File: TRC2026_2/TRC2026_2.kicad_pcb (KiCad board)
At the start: 2 copper layers, 79 x 180 mm, 31 parts, among them J1 Conn_01x02_Pin, J15 Conn_01x04_Pin, J16 デジタル電圧計(測定), J17 デジタル電圧計(電力供給), J2 Conn_01x04_Pin, J3 Conn_01x04_Pin, J4 Conn_01x04_Pin, J5 Conn_01x04_Pin, SW1 SW_SPST, SW2 SW_SPDT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

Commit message: 基板をめちゃめちゃ修正しました
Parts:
- added G***: LOGO, LOGO, F.Cu at (123.0, 124.0)
- added J6: Conn_01x04_Pin, Connector_PinHeader_2.54mm:PinHeader_1x04_P2.54mm_Vertical, F.Cu at (106.8, 42.8)
- moved D8 2.50 mm to (89.0, 185.0)
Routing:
- net +24V: track 235.5 -> 409.3 mm, vias 0 -> 2
- net GND: track 0.00 -> 4.29 mm, vias 0 -> 1
- net Net-(U1-EN): track 37.0 -> 39.2 mm
- net +5V: track 276.5 -> 274.8 mm
- net Net-(D8-K): track 72.6 -> 73.9 mm
- net Net-(J1-Pin_1): track 32.3 -> 32.9 mm
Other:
- board text added: "SBD"
- board text added: "TRC_Noname 2F"
- board text added: "緑色LED"
- board text added: "赤色LED"
- board text added: "青色LED"

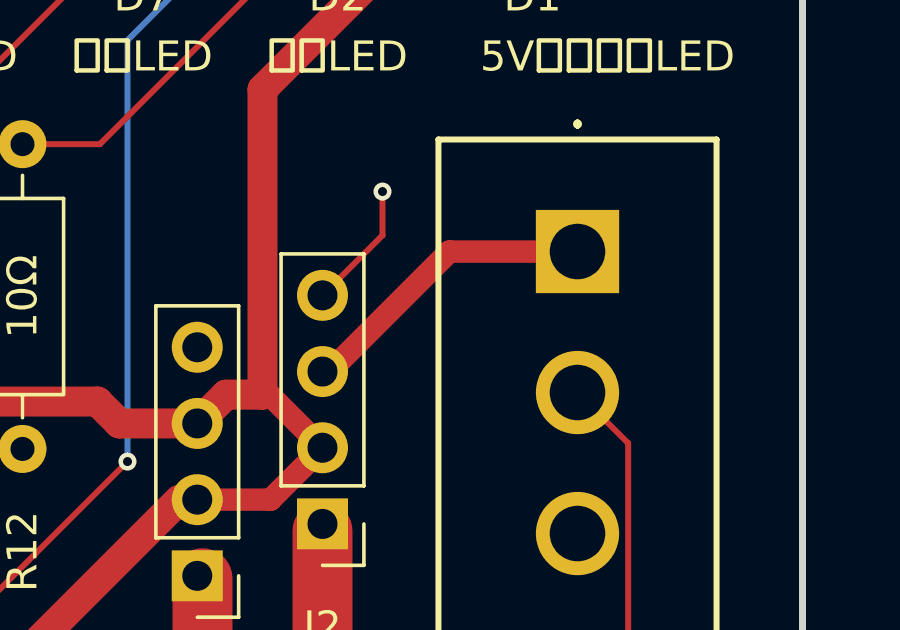
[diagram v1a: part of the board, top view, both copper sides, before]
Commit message: プルダウン抵抗とフットプリントを修正しました
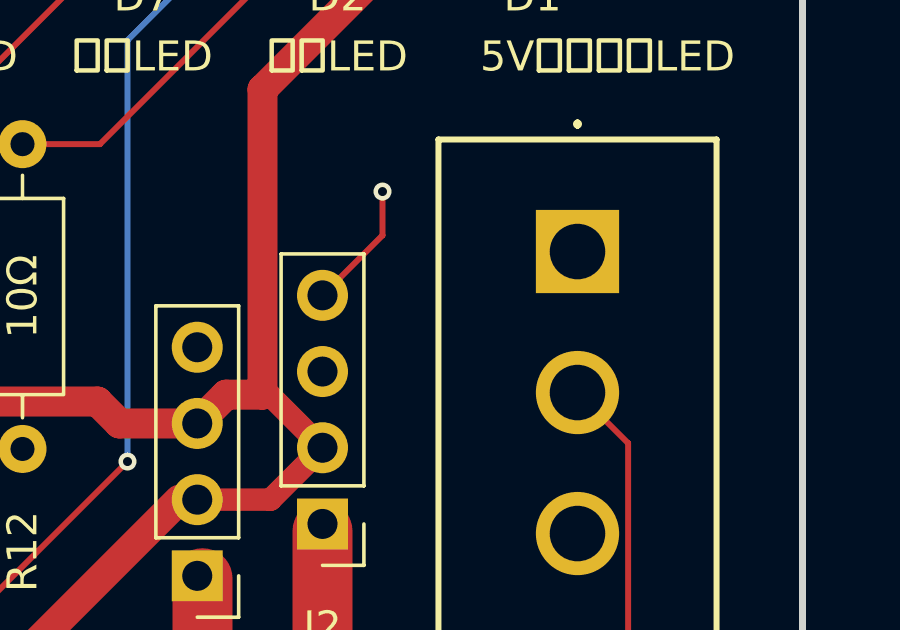
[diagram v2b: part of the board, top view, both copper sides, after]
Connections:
- SW2 pad 1: +3.3V -> unconnected-(SW2-A-Pad1)
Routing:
- net +3.3V: track 10.3 -> 0.00 mm
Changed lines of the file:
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@@
 	(net 24 "unconnected-(U1-PG-Pad3)")
 	(net 25 "unconnected-(U1-NC-Pad5)")
+	(net 26 "unconnected-(SW2-A-Pad1)")
 	(footprint "3557-15:FUSE_3557-15"
 		(layer "F.Cu")
@@
 			(layers "*.Cu" "*.Mask")
 			(remove_unused_layers no)
-			(net 19 "+3.3V")
+			(net 26 "unconnected-(SW2-A-Pad1)")
 			(pinfunction "A")
-			(pintype "passive")
+			(pintype "passive+no_connect")
 		)
 		(pad "2" thru_hole circle
@@
 	)
 	(segment
-		(start 111 36.23)
-		(end 115.23 32)
-		(width 0.75)
-		(layer "F.Cu")
-		(net 19)
-	)
-	(segment
-		(start 115.23 32)
-		(end 119.5 32)
-		(width 0.75)
-		(layer "F.Cu")
-		(net 19)
-	)
-	(segment
